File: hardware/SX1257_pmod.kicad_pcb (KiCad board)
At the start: 4 copper layers, 20.3 x 45.5 mm, 45 parts, among them J1 Conn_02x06_Odd_Even, J2 SMA_F_RX, J3 SMA_F_TX, U1 SX1257, U2 SC18IS602B, Y1 36MHz 10ppm

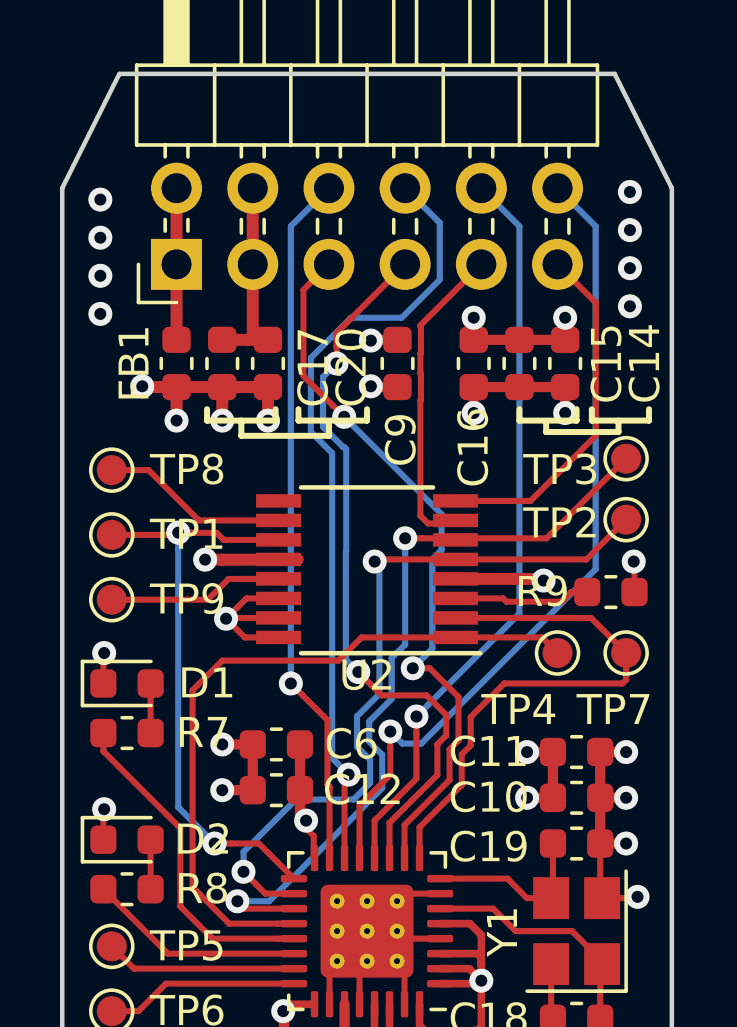
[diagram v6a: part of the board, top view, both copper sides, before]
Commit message: Swap pmod rows and add pull-ups.
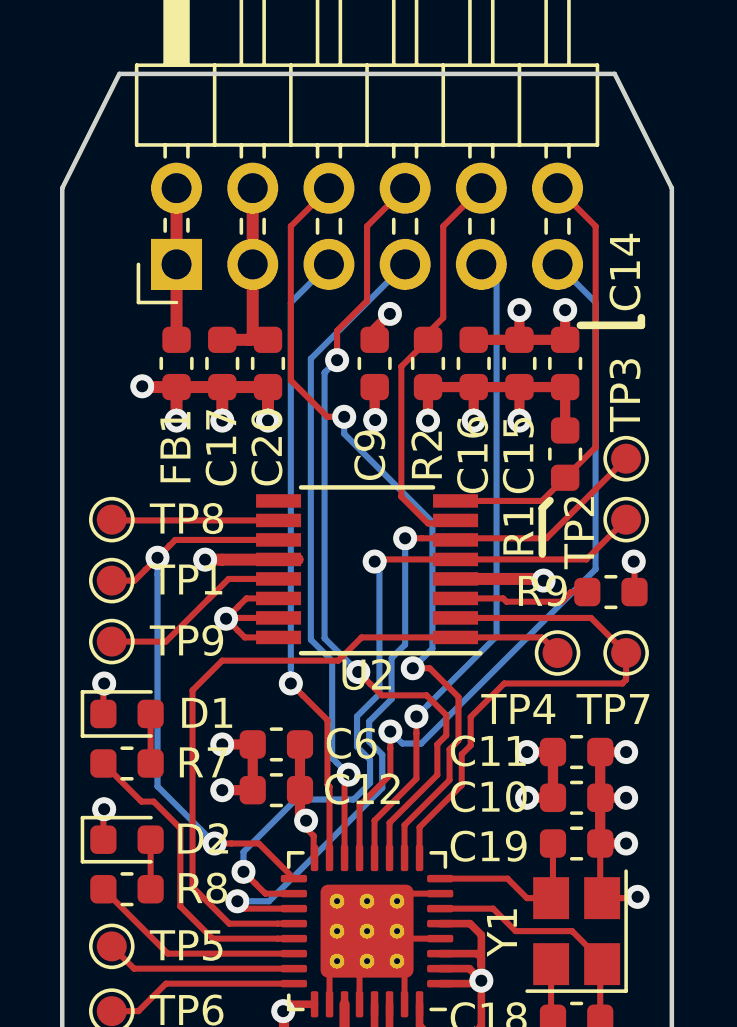
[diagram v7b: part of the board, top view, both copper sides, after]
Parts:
- added R1: 2k2, Resistor_SMD:R_0603_1608Metric, F.Cu at (131.1, 35.5)
- added R2: 2k2, Resistor_SMD:R_0603_1608Metric, F.Cu at (126.5, 32.5)
- moved LOGO1 8.07 mm to (130.2, 56.9)
- moved TP8 1.65 mm to (116.0, 37.7)
- moved TP1 1.52 mm to (116.0, 39.8)
- moved TP9 1.40 mm to (116.0, 41.8)
- moved D1 1.02 mm to (116.5, 44.2)
- moved R7 1.02 mm to (116.5, 45.8)
- moved C9 0.76 mm to (124.7, 32.5), turned to 90 degrees
- turned C14 to 90 degrees
- turned C15 to 90 degrees
- turned C16 to 90 degrees
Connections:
- J1 pad 10: /PMOD_6 -> /I2C_SDA
- J1 pad 11: /I2C_CLK -> /I_IN
- J1 pad 12: /PMOD_5 -> /I2C_SCL
- J1 pad 5: /CLK_OUT -> /I_OUT
- J1 pad 6: /PMOD_8 -> /CLK_OUT
- J1 pad 7: /CLK_IN -> /PMOD_3
- J1 pad 8: /PMOD_7 -> /CLK_IN
- J1 pad 9: /I2C_SDA -> /PMOD_2
- U1 pad 12: /PMOD_6 -> /PMOD_2
- U1 pad 13: /PMOD_5 -> /I_IN
- U1 pad 14: /PMOD_7 -> /PMOD_3
- U1 pad 15: /PMOD_8 -> /I_OUT
- U2 pad 8: /I2C_CLK -> /I2C_SCL
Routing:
- net /PMOD_5: track 27.3 -> 0.00 mm, vias 1 -> 0
- net /PMOD_7: track 26.2 -> 0.00 mm, vias 1 -> 0
- net /PMOD_6: track 24.9 -> 0.00 mm, vias 1 -> 0
- net /I_IN: track 0.00 -> 24.7 mm, vias 0 -> 1
- net /PMOD_8: track 23.4 -> 0.00 mm, vias 1 -> 0
- net /PMOD_2: track 0.00 -> 21.7 mm, vias 0 -> 1
- net /PMOD_3: track 0.00 -> 21.7 mm, vias 0 -> 1
- net /I_OUT: track 0.00 -> 20.8 mm, vias 0 -> 1
- net /I2C_SCL: track 0.00 -> 13.9 mm
- net /I2C_CLK: track 11.2 -> 0.00 mm
- net +3V3: track 38.9 -> 44.0 mm, vias 14 -> 15
- net /I2C_SDA: track 11.2 -> 14.2 mm
- net /CLK_OUT: track 24.2 -> 27.1 mm
- net /CLK_IN: track 24.3 -> 26.8 mm
- net /GPIO2: track 6.89 -> 5.57 mm
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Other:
- net class Default: trace_width 0.1524 -> 0.2032
- board text added: "+3V3"
- board text added: "CLK_IN"
- board text added: "CLK_OUT"
- board text added: "GND"
- board text added: "I2C_SCL"
- board text added: "I2C_SDA"
- board text added: "I_IN"
- board text added: "I_OUT"
- board text added: "Q_IN"
- board text added: "Q_OUT"
- board text added: "SX1257 PMOD RevB 2019-03"
- board text removed: "SX1257 PMOD 2019-01 RevA @kbeckmann @ico_TC @tnt"

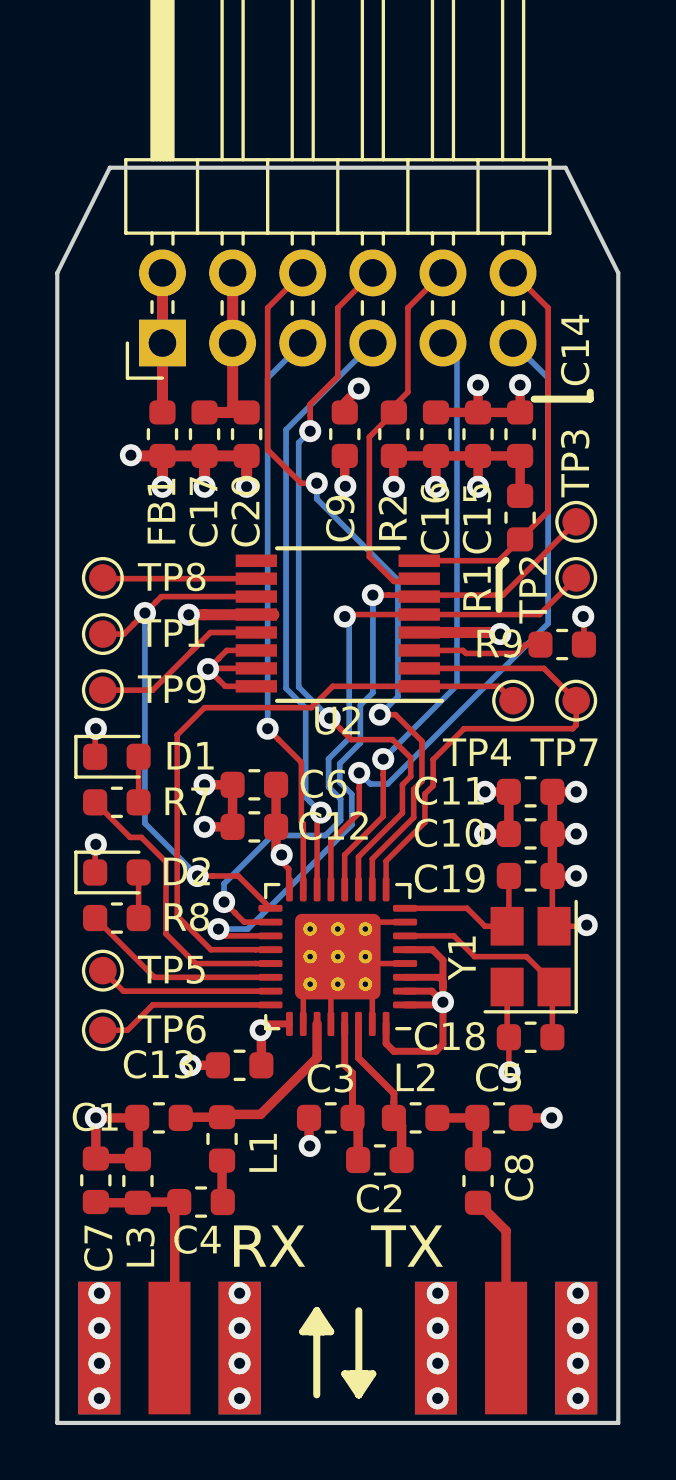
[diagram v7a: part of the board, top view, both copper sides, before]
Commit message: RevB improvements
- Clean up routing and improve ground plane
- Change crystal to 1.6x1.2mm
- Minor improvements everywhere
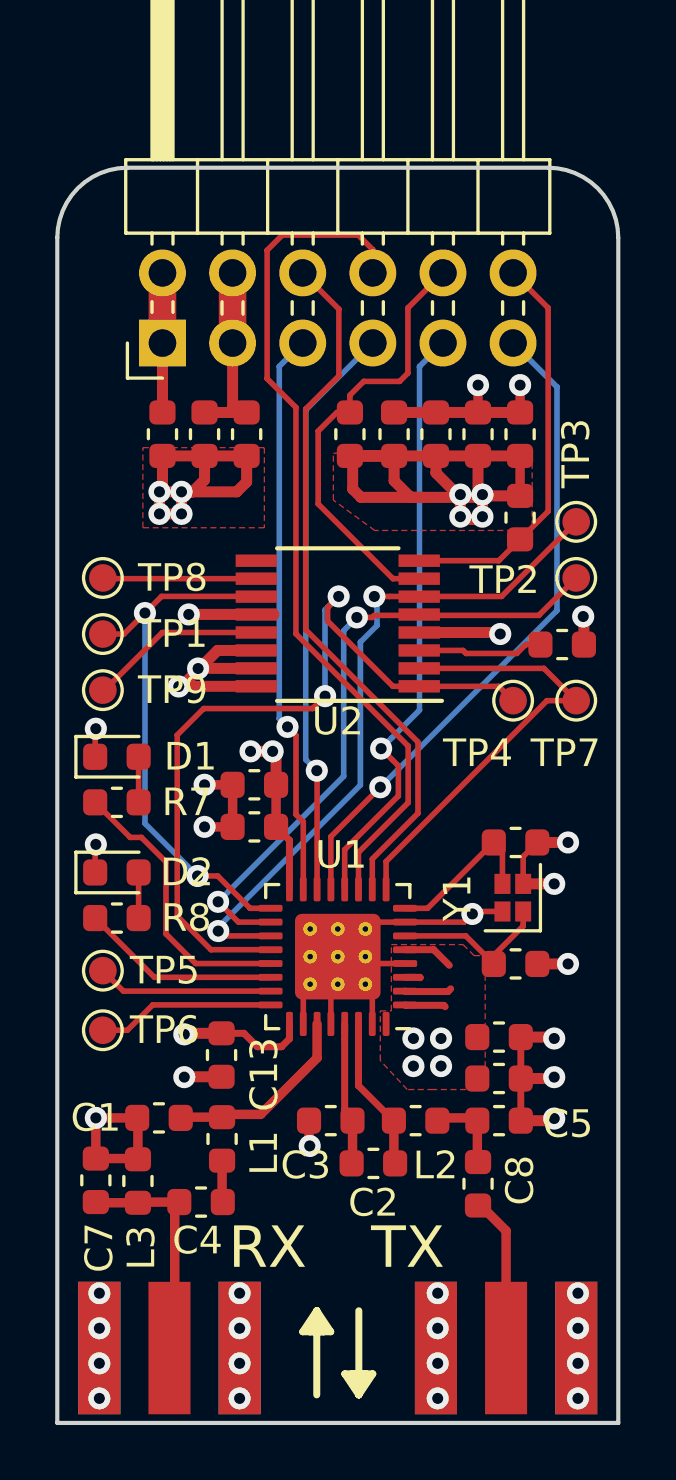
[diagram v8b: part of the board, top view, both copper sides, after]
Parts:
- Y1: footprint Crystal:Crystal_SMD_3225-4Pin_3.2x2.5mm -> extra:Crystal_SMD_1612-4Pin_1.6x1.2mm
- moved LOGO1 16.8 mm to (118.0, 45.3)
- moved C11 8.96 mm to (130.3, 54.4)
- moved C10 8.93 mm to (130.3, 55.9)
- moved C18 2.71 mm to (130.9, 51.7), turned to 0 degrees
- moved Y1 2.23 mm to (130.8, 49.3)
- moved C9 1.79 mm to (126.5, 32.5)
- moved R2 1.59 mm to (124.9, 32.5)
- moved C19 1.33 mm to (130.9, 47.3)
- moved C13 0.75 mm to (120.2, 55.0), turned to 270 degrees
- moved C2 0.26 mm to (125.8, 58.9)
- moved C3 0.10 mm to (124.2, 57.4)
- moved C5 0.10 mm to (130.3, 57.4)
- moved L2 0.10 mm to (127.3, 57.4)
- moved C8 0.10 mm to (129.5, 59.7)
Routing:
- net +3V3: track 44.0 -> 58.0 mm, vias 15 -> 17
- net GND: track 75.8 -> 82.5 mm, vias 34 -> 35
- net /SPI_NSS: track 23.6 -> 28.5 mm, vias 0 -> 2
- net /CLK_IN: track 26.8 -> 31.1 mm, vias 2 -> 0
- net /I2C_SDA: track 14.2 -> 17.1 mm
- net /XTA: track 8.07 -> 5.98 mm
- net /SX_RESET: track 17.5 -> 15.8 mm
- net /SPI_MISO: track 24.7 -> 23.1 mm
- net /CLK_OUT: track 27.1 -> 25.7 mm, vias 2 -> 0
- net /SPI_MOSI: track 25.8 -> 24.9 mm
- net /I_IN: track 24.7 -> 23.8 mm
- net /PMOD_3: track 21.7 -> 21.0 mm
- added copper zone on F.Cu, net +3V3
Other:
- outline, holes or cut-outs redrawn
- board text added: "SX1257 PMOD RevB 2019-05"
- board text added: "https://git.xil.se/kbeckmann/SX1257"
- board text removed: "SX1257 PMOD RevB 2019-03"
